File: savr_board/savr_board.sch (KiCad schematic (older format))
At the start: 7 parts, among them J1 SATA-7, J2 SATA-7, J3 SATA-7, J4 SATA-7, U1 XC7Z030-CLG485, U2 DDR3_256Mx16, U3 DDR3_256Mx16

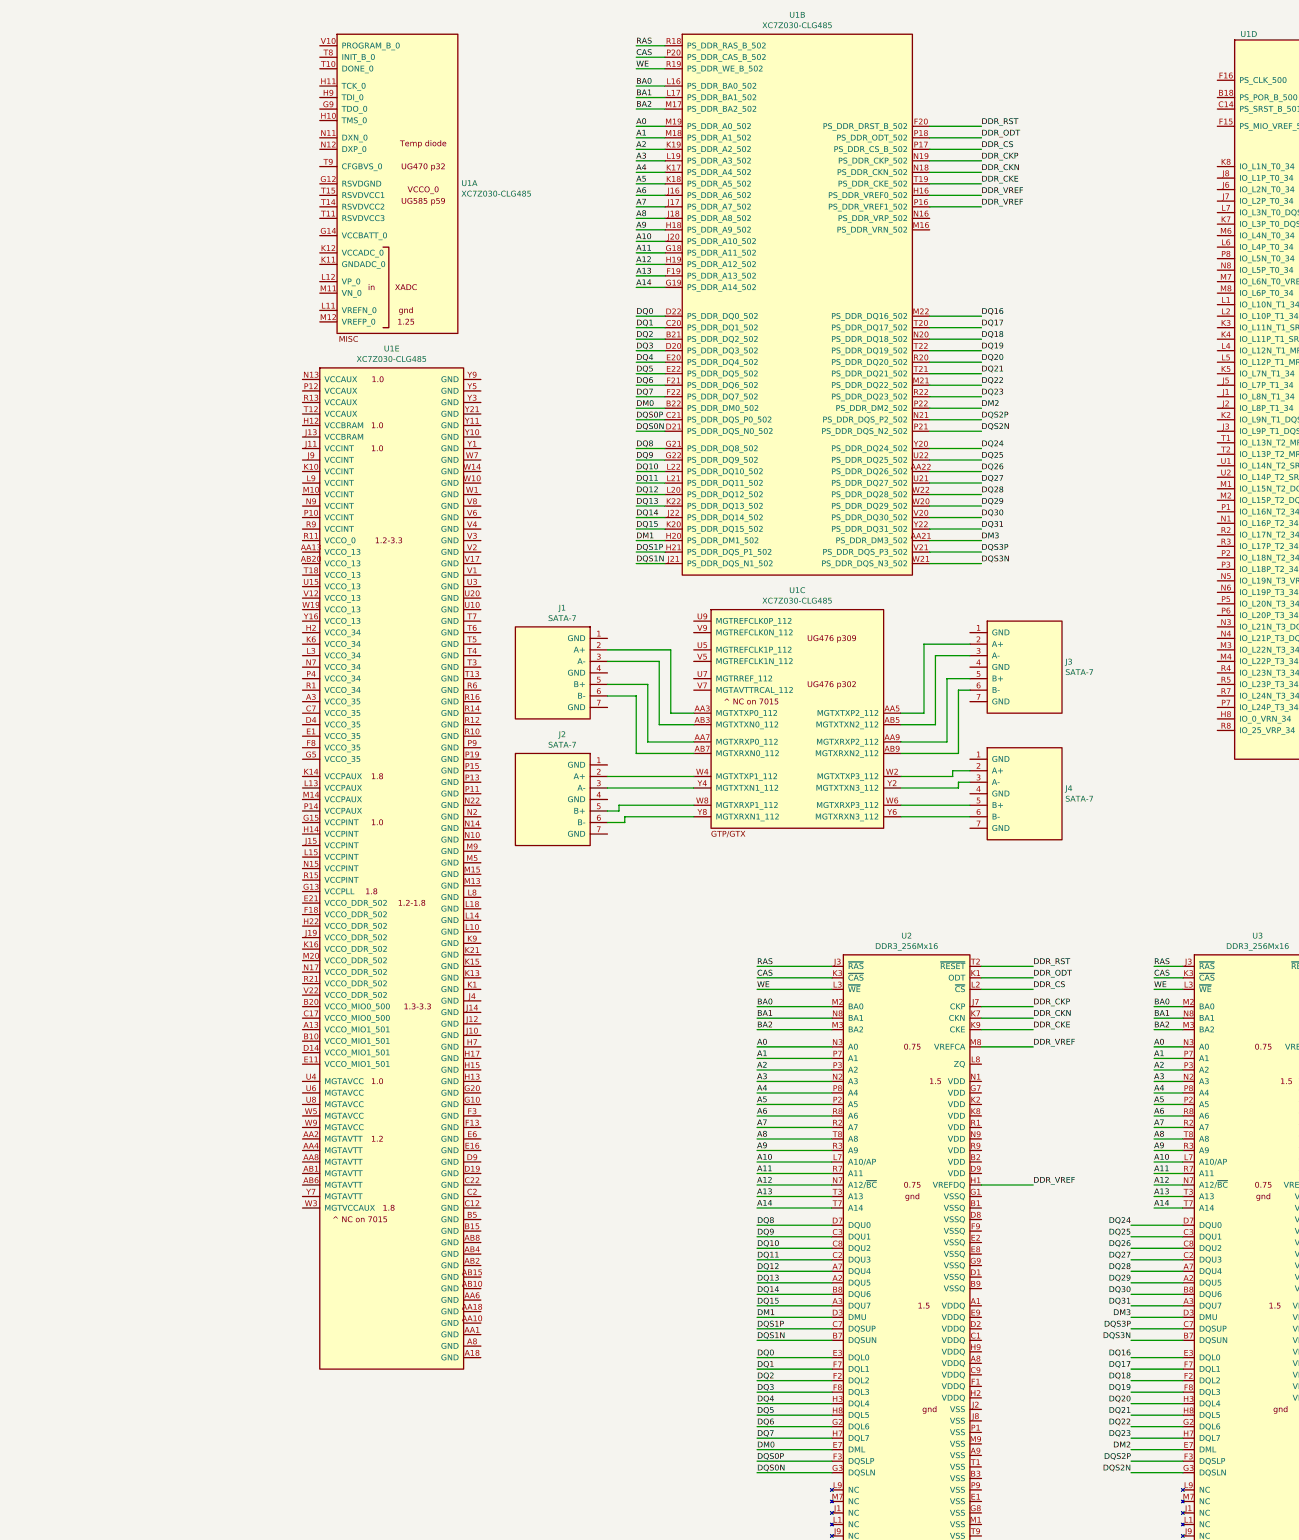
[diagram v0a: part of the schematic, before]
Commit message: Escape routing for the first 5 rows, not paying special attention to differentials
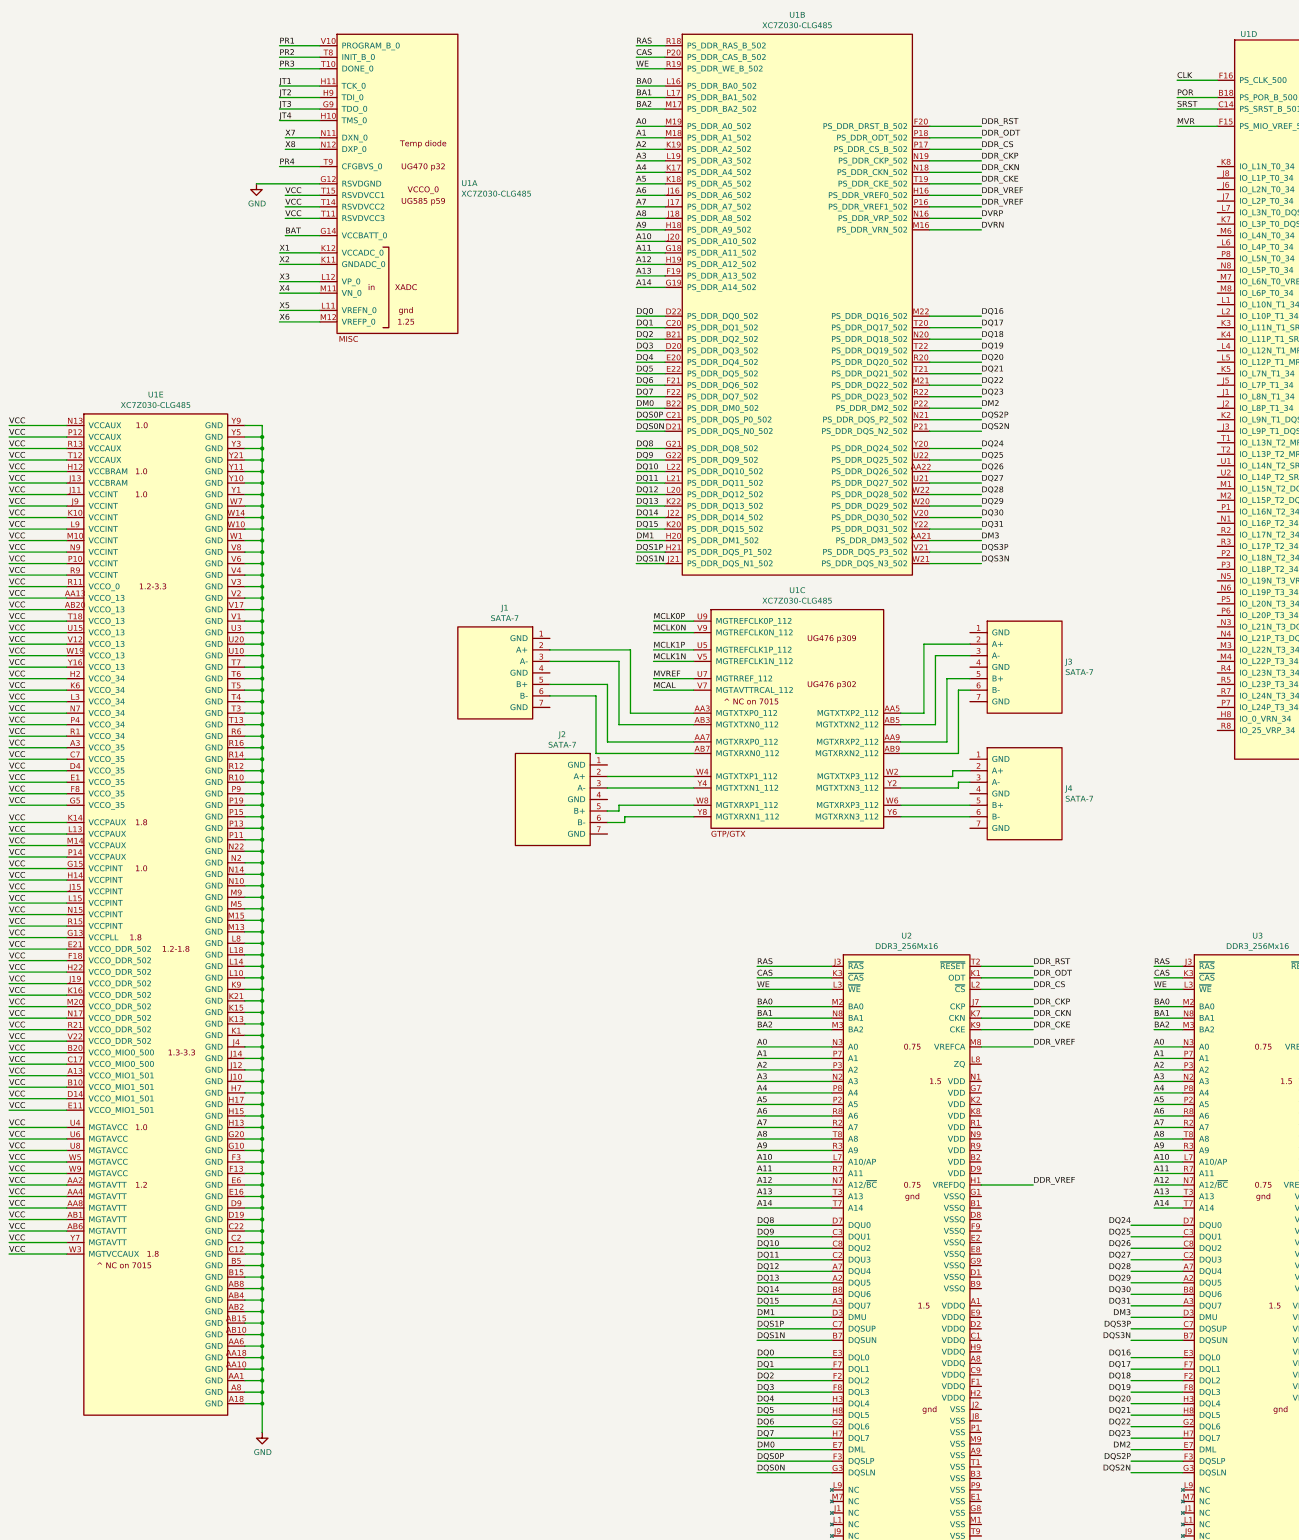
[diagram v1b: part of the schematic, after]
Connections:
- net GND: now reaches U1.G12 (RSVDGND)
- net GND: now also U1.A18 (GND), U1.A8 (GND), U1.AA1 (GND), U1.AA10 (GND), U1.AA18 (GND), U1.AA6 (GND), U1.AB10 (GND), U1.AB15 (GND), U1.AB2 (GND), U1.AB4 (GND), U1.AB8 (GND), U1.B15 (GND), U1.B5 (GND), U1.C12 (GND), U1.C2 (GND), U1.C22 (GND), U1.D19 (GND), U1.D9 (GND), U1.E16 (GND), U1.E6 (GND), U1.F13 (GND), U1.F3 (GND), U1.G10 (GND), U1.G20 (GND), U1.H13 (GND), U1.H15 (GND), U1.H17 (GND), U1.H7 (GND), U1.J10 (GND), U1.J12 (GND), U1.J14 (GND), U1.J4 (GND), U1.K1 (GND), U1.K13 (GND), U1.K15 (GND), U1.K21 (GND), U1.K9 (GND), U1.L10 (GND), U1.L14 (GND), U1.L18 (GND), U1.L8 (GND), U1.M13 (GND), U1.M15 (GND), U1.M5 (GND), U1.M9 (GND), U1.N10 (GND), U1.N14 (GND), U1.N2 (GND), U1.N22 (GND), U1.P11 (GND), U1.P13 (GND), U1.P15 (GND), U1.P19 (GND), U1.P9 (GND), U1.R10 (GND), U1.R12 (GND), U1.R14 (GND), U1.R16 (GND), U1.R6 (GND), U1.T13 (GND), U1.T3 (GND), U1.T4 (GND), U1.T5 (GND), U1.T6 (GND), U1.T7 (GND), U1.U10 (GND), U1.U20 (GND), U1.U3 (GND), U1.V1 (GND), U1.V17 (GND), U1.V2 (GND), U1.V3 (GND), U1.V4 (GND), U1.V6 (GND), U1.V8 (GND), U1.W1 (GND), U1.W10 (GND), U1.W14 (GND), U1.W7 (GND), U1.Y1 (GND), U1.Y10 (GND), U1.Y11 (GND), U1.Y21 (GND), U1.Y3 (GND), U1.Y5 (GND), U1.Y9 (GND)
- net BAT: now reaches U1.G14 (VCCBATT_0)
- net JT3: now reaches U1.G9 (TDO_0)
- net JT4: now reaches U1.H10 (TMS_0)
- net JT1: now reaches U1.H11 (TCK_0)
- net JT2: now reaches U1.H9 (TDI_0)
- net X2: now reaches U1.K11 (GNDADC_0)
- net X1: now reaches U1.K12 (VCCADC_0)
- net X5: now reaches U1.L11 (VREFN_0)
- net X3: now reaches U1.L12 (VP_0)
- net X4: now reaches U1.M11 (VN_0)
- net X6: now reaches U1.M12 (VREFP_0)
- net X7: now reaches U1.N11 (DXN_0)
- net X8: now reaches U1.N12 (DXP_0)
- net PR3: now reaches U1.T10 (DONE_0)
- net VCC: now reaches U1.T11 (RSVDVCC3)
- net VCC: now also U1.A13 (VCCO_MIO1_501), U1.A3 (VCCO_35), U1.AA13 (VCCO_13), U1.AA2 (MGTAVTT), U1.AA4 (MGTAVTT), U1.AA8 (MGTAVTT), U1.AB1 (MGTAVTT), U1.AB20 (VCCO_13), U1.AB6 (MGTAVTT), U1.B10 (VCCO_MIO1_501), U1.B20 (VCCO_MIO0_500), U1.C17 (VCCO_MIO0_500), U1.C7 (VCCO_35), U1.D14 (VCCO_MIO1_501), U1.D4 (VCCO_35), U1.E1 (VCCO_35), U1.E11 (VCCO_MIO1_501), U1.E21 (VCCO_DDR_502), U1.F18 (VCCO_DDR_502), U1.F8 (VCCO_35), U1.G13 (VCCPLL), U1.G15 (VCCPINT), U1.G5 (VCCO_35), U1.H12 (VCCBRAM), U1.H14 (VCCPINT), U1.H2 (VCCO_34), U1.H22 (VCCO_DDR_502), U1.J11 (VCCINT), U1.J13 (VCCBRAM), U1.J15 (VCCPINT), U1.J19 (VCCO_DDR_502), U1.J9 (VCCINT), U1.K10 (VCCINT), U1.K14 (VCCPAUX), U1.K16 (VCCO_DDR_502), U1.K6 (VCCO_34), U1.L13 (VCCPAUX), U1.L15 (VCCPINT), U1.L3 (VCCO_34), U1.L9 (VCCINT), U1.M10 (VCCINT), U1.M14 (VCCPAUX), U1.M20 (VCCO_DDR_502), U1.N13 (VCCAUX), U1.N15 (VCCPINT), U1.N17 (VCCO_DDR_502), U1.N7 (VCCO_34), U1.N9 (VCCINT), U1.P10 (VCCINT), U1.P12 (VCCAUX), U1.P14 (VCCPAUX), U1.P4 (VCCO_34), U1.R1 (VCCO_34), U1.R11 (VCCO_0), U1.R13 (VCCAUX), U1.R15 (VCCPINT), U1.R21 (VCCO_DDR_502), U1.R9 (VCCINT), U1.T12 (VCCAUX), U1.T14 (RSVDVCC2), U1.T15 (RSVDVCC1), U1.T18 (VCCO_13), U1.U15 (VCCO_13), U1.U4 (MGTAVCC), U1.U6 (MGTAVCC), U1.U8 (MGTAVCC), U1.V12 (VCCO_13), U1.V22 (VCCO_DDR_502), U1.W19 (VCCO_13), U1.W3 (MGTVCCAUX), U1.W5 (MGTAVCC), U1.W9 (MGTAVCC), U1.Y16 (VCCO_13), U1.Y7 (MGTAVTT)
- net PR2: now reaches U1.T8 (INIT_B_0)
- net PR4: now reaches U1.T9 (CFGBVS_0)
- net PR1: now reaches U1.V10 (PROGRAM_B_0)
- net DVRN: now reaches U1.M16 (PS_DDR_VRN_502)
- net DVRP: now reaches U1.N16 (PS_DDR_VRP_502)
- net MCLK1P: now reaches U1.U5 (MGTREFCLK1P_112)
- net MVREF: now reaches U1.U7 (MGTRREF_112)
- net MCLK0P: now reaches U1.U9 (MGTREFCLK0P_112)
- net MCLK1N: now reaches U1.V5 (MGTREFCLK1N_112)
- net MCAL: now reaches U1.V7 (MGTAVTTRCAL_112)
- net MCLK0N: now reaches U1.V9 (MGTREFCLK0N_112)
- net POR: now reaches U1.B18 (PS_POR_B_500)
- net SRST: now reaches U1.C14 (PS_SRST_B_501)
- net MVR: now reaches U1.F15 (PS_MIO_VREF_501)
- net CLK: now reaches U1.F16 (PS_CLK_500)
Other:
- moved on the sheet: J1, U1E

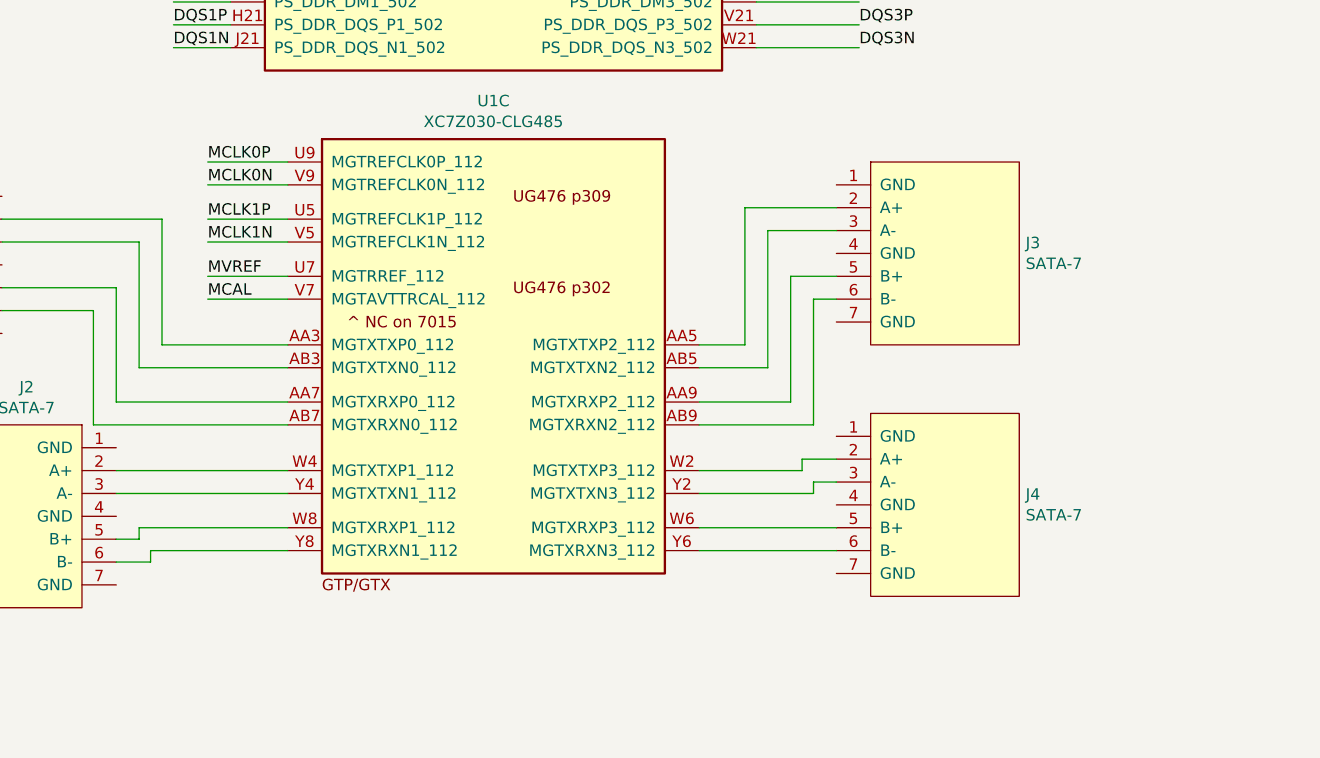
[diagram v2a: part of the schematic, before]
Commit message: Feasibility test of IO connectors and SATA routing
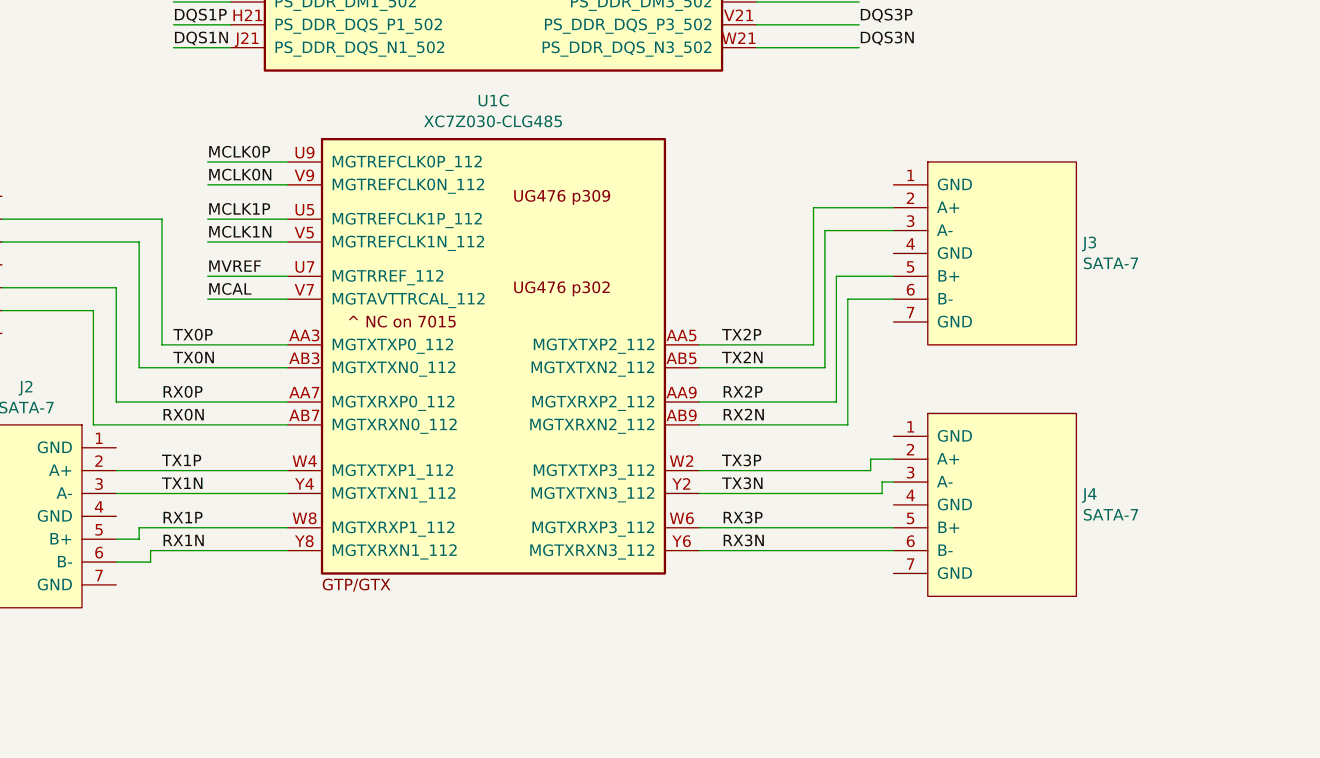
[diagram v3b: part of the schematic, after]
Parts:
- J1, J2, J3, J4: footprint savr_board:SATA-7 -> savr_board:SATA-7-SMD-vert
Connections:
- net TX0P: now reaches J1.2 (A+), U1.AA3 (MGTXTXP0_112)
- net TX2P: now reaches J3.2 (A+), U1.AA5 (MGTXTXP2_112)
- net RX0P: now reaches J1.5 (B+), U1.AA7 (MGTXRXP0_112)
- net RX2P: now reaches J3.5 (B+), U1.AA9 (MGTXRXP2_112)
- net TX0N: now reaches J1.3 (A-), U1.AB3 (MGTXTXN0_112)
- net TX2N: now reaches J3.3 (A-), U1.AB5 (MGTXTXN2_112)
- net RX0N: now reaches J1.6 (B-), U1.AB7 (MGTXRXN0_112)
- net RX2N: now reaches J3.6 (B-), U1.AB9 (MGTXRXN2_112)
- net TX3P: now reaches J4.2 (A+), U1.W2 (MGTXTXP3_112)
- net TX1P: now reaches J2.2 (A+), U1.W4 (MGTXTXP1_112)
- net RX3P: now reaches J4.5 (B+), U1.W6 (MGTXRXP3_112)
- net RX1P: now reaches J2.5 (B+), U1.W8 (MGTXRXP1_112)
- net TX3N: now reaches J4.3 (A-), U1.Y2 (MGTXTXN3_112)
- net TX1N: now reaches J2.3 (A-), U1.Y4 (MGTXTXN1_112)
- net RX3N: now reaches J4.6 (B-), U1.Y6 (MGTXRXN3_112)
- net RX1N: now reaches J2.6 (B-), U1.Y8 (MGTXRXN1_112)
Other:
- moved on the sheet: J3, J4
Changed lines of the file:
@@
 F 0 "J1" H 2042 6015 50  0000 C CNN
 F 1 "SATA-7" H 2042 5924 50  0000 C CNN
-F 2 "savr_board:SATA-7" H 1650 5850 50  0001 C CNN
+F 2 "savr_board:SATA-7-SMD-vert" H 1650 5850 50  0001 C CNN
 F 3 "" H 1650 5850 50  0001 C CNN
 	1    1800 5850
@@
 F 0 "J2" H 2542 7115 50  0000 C CNN
 F 1 "SATA-7" H 2542 7024 50  0000 C CNN
-F 2 "savr_board:SATA-7" H 2150 6950 50  0001 C CNN
+F 2 "savr_board:SATA-7-SMD-vert" H 2150 6950 50  0001 C CNN
 F 3 "" H 2150 6950 50  0001 C CNN
 	1    2300 6950
@@
 L savr_symbols:SATA-7 J3
 U 1 1 5CD3A8CD
-P 5750 5800
-F 0 "J3" H 6428 5446 50  0000 L CNN
-F 1 "SATA-7" H 6428 5355 50  0000 L CNN
-F 2 "savr_board:SATA-7" H 5600 5800 50  0001 C CNN
-F 3 "" H 5600 5800 50  0001 C CNN
-	1    5750 5800
+P 6000 5800
+F 0 "J3" H 6678 5446 50  0000 L CNN
+F 1 "SATA-7" H 6678 5355 50  0000 L CNN
+F 2 "savr_board:SATA-7-SMD-vert" H 5850 5800 50  0001 C CNN
+F 3 "" H 5850 5800 50  0001 C CNN
+	1    6000 5800
 	1    0    0    -1
 $EndComp
@@
 L savr_symbols:SATA-7 J4
 U 1 1 5CD3C2FC
-P 5750 6900
-F 0 "J4" H 6428 6546 50  0000 L CNN
-F 1 "SATA-7" H 6428 6455 50  0000 L CNN
-F 2 "savr_board:SATA-7" H 5600 6900 50  0001 C CNN
-F 3 "" H 5600 6900 50  0001 C CNN
-	1    5750 6900
+P 6000 6900
+F 0 "J4" H 6678 6546 50  0000 L CNN
+F 1 "SATA-7" H 6678 6455 50  0000 L CNN
+F 2 "savr_board:SATA-7-SMD-vert" H 5850 6900 50  0001 C CNN
+F 3 "" H 5850 6900 50  0001 C CNN
+	1    6000 6900
 	1    0    0    -1
 $EndComp
@@
 	2600 7550 2450 7550
 Wire Wire Line
-	5000 7500 5600 7500
-Wire Wire Line
-	5000 7400 5600 7400
-Wire Wire Line
-	5000 7250 5500 7250
-Wire Wire Line
-	5500 7250 5500 7200
-Wire Wire Line
-	5500 7200 5600 7200
-Wire Wire Line
-	5000 7150 5450 7150
-Wire Wire Line
-	5450 7150 5450 7100
-Wire Wire Line
-	5450 7100 5600 7100
-Wire Wire Line
-	5000 6950 5500 6950
-Wire Wire Line
-	5500 6950 5500 6400
-Wire Wire Line
-	5500 6400 5600 6400
-Wire Wire Line
-	5000 6850 5400 6850
-Wire Wire Line
-	5400 6850 5400 6300
-Wire Wire Line
-	5400 6300 5600 6300
-Wire Wire Line
-	5000 6700 5300 6700
-Wire Wire Line
-	5300 6700 5300 6100
-Wire Wire Line
-	5300 6100 5600 6100
-Wire Wire Line
-	5000 6600 5200 6600
-Wire Wire Line
-	5200 6600 5200 6000
-Wire Wire Line
-	5200 6000 5600 6000
+	5000 7500 5850 7500
+Wire Wire Line
+	5000 7400 5850 7400
+Wire Wire Line
+	5000 6950 5650 6950
+Wire Wire Line
+	5650 6950 5650 6400
+Wire Wire Line
+	5650 6400 5850 6400
+Wire Wire Line
+	5000 6850 5600 6850
+Wire Wire Line
+	5600 6850 5600 6300
+Wire Wire Line
+	5600 6300 5850 6300
+Wire Wire Line
+	5000 6700 5550 6700
+Wire Wire Line
+	5550 6700 5550 6100
+Wire Wire Line
+	5550 6100 5850 6100
+Wire Wire Line
+	5000 6600 5500 6600
+Wire Wire Line
+	5500 6600 5500 6000
+Wire Wire Line
+	5500 6000 5850 6000
 Wire Wire Line
 	-2250 4100 -2750 4100
@@
 VCC
 $Comp
-L power:GND #PWR?
+L power:GND #PWR0102
 U 1 1 5D363AE4
 P -600 2000
-F 0 "#PWR?" H -600 1750 50  0001 C CNN
+F 0 "#PWR0102" H -600 1750 50  0001 C CNN
 F 1 "GND" H -595 1827 50  0000 C CNN
 F 2 "" H -600 2000 50  0001 C CNN
@@
 	1    0    0    -1
 $EndComp
+Text Label 2700 6600 0    50   ~ 0
+TX0P
+Text Label 2700 6700 0    50   ~ 0
+TX0N
+Text Label 2650 6850 0    50   ~ 0
+RX0P
+Text Label 2650 6950 0    50   ~ 0
+RX0N
+Text Label 2650 7150 0    50   ~ 0
+TX1P
+Text Label 2650 7250 0    50   ~ 0
+TX1N
+Text Label 2650 7400 0    50   ~ 0
+RX1P
+Text Label 2650 7500 0    50   ~ 0
+RX1N
+Wire Wire Line
+	5000 7250 5800 7250
+Wire Wire Line
+	5800 7250 5800 7200
+Wire Wire Line
+	5800 7200 5850 7200
+Wire Wire Line
+	5000 7150 5750 7150
+Wire Wire Line
+	5750 7150 5750 7100
+Wire Wire Line
+	5750 7100 5850 7100
+Text Label 5100 6600 0    50   ~ 0
+TX2P
+Text Label 5100 6700 0    50   ~ 0
+TX2N
+Text Label 5100 6850 0    50   ~ 0
+RX2P
+Text Label 5100 6950 0    50   ~ 0
+RX2N
+Text Label 5100 7150 0    50   ~ 0
+TX3P
+Text Label 5100 7250 0    50   ~ 0
+TX3N
+Text Label 5100 7400 0    50   ~ 0
+RX3P
+Text Label 5100 7500 0    50   ~ 0
+RX3N
 $EndSCHEMATC
